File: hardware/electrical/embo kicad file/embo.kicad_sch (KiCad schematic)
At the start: 107 parts, among them J1 24 V PSU input, J10 Conn_01x14, J11 Conn_01x03, J12 Conn_Coaxial, J13 LED Panel, J14 Conn_Coaxial, J2 USB_C_Receptacle_USB2.0_16P, J3 Motor 1 coil A, J4 Motor 1 coil B, J5 Motor 2 coil A, J6 Motor 2 coil B, J7 raspberry pi UART, J8 motor 1, J9 motor 2, Q1 AO3401, U1 TMC2209-LA, U2 ESP32-S3-WROOM-1, U3 AMS1117-3.3, U4 TMC2209-LA, U5 LM2596S-5, U6 OPA2354, U7 OPA2354, U8 AD9833xRM

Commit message: updated
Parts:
- removed Q1: AO3401, symbol Transistor_FET:Q_PMOS_GSD
- added Q2: AO4407A, AO4407A:SOIC127P600X175-8N, symbol AO4407A:AO4407A
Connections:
- net at R5.1: now also Q2.4
- net at J1.1 (Pin_1): now also Q2.5, Q2.6, Q2.7, Q2.8
- net at D1.2 (A), F1.1: now also Q2.1, Q2.2, Q2.3
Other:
- moved on the sheet: R5

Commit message: schematic and pcb docs update
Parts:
- removed J3: Motor 1 coil A, symbol Connector_Generic:Conn_01x02
- removed J4: Motor 1 coil B, symbol Connector_Generic:Conn_01x02
- removed J5: Motor 2 coil A, symbol Connector_Generic:Conn_01x02
- removed J6: Motor 2 coil B, symbol Connector_Generic:Conn_01x02
- added J3, J4: Conn_01x06_Socket, symbol Connector:Conn_01x06_Socket
- Q2: footprint AO4407A:SOIC127P600X175-8N -> Package_SO:SOIC-8_3.9x4.9mm_P1.27mm
- U6, U7: footprint OPA2354AQDGKRQ1:SOP65P490X110-8N -> Package_SO:SOIC-8_3.9x4.9mm_P1.27mm

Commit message: update schematic and PCb docs
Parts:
- removed 10Ω111: R, symbol Device:R
- removed 1nF1: C, symbol Device:C
- removed C1, C2, C3, C6, C8, C9: 100nF, symbol Device:C
- removed C4, C5: 100µF, symbol Device:C
- removed D1: D_Zener, symbol Device:D_Zener
- removed J1: 24 V PSU input, symbol Connector_Generic:Conn_01x02
- removed J11: Conn_01x03, symbol Connector_Generic:Conn_01x03
- removed J7: raspberry pi UART, symbol Connector_Generic:Conn_01x04
- removed R10, R11, R14, R23, R24: 10kΩ, symbol Device:R
- added C36: 100µF, symbol Device:C
- added C37, C40, C41: 100nF, Capacitor_SMD:C_0402_1005Metric, symbol Device:C
- added C38, C39: 100uF, symbol Device:C_Polarized
- added C50: 1nF, Capacitor_SMD:C_0402_1005Metric, symbol Device:C
- added D5: SMBJ28A, Diode_SMD:D_SMA, symbol Device:D_Zener
- added D7: BZX84C15, Package_TO_SOT_SMD:SOT-23, symbol Device:D_Zener
- added J10: BTN UP, Connector_JST:JST_XH_B2B-XH-A_1x02_P2.50mm_Vertical, symbol Connector_Generic:Conn_01x02
- added J11: BTN DOWN, Connector_JST:JST_XH_B2B-XH-A_1x02_P2.50mm_Vertical, symbol Connector_Generic:Conn_01x02
- added J12: BTN SELECT, Connector_JST:JST_XH_B2B-XH-A_1x02_P2.50mm_Vertical, symbol Connector_Generic:Conn_01x02
- added J14: 24 V PSU input, TerminalBlock_Phoenix:TerminalBlock_Phoenix_PT-1,5-2-3.5-H_1x02_P3.50mm_Horizontal, symbol Connector_Generic:Conn_01x02
- added J3: UART to RPi, Connector_JST:JST_XH_B3B-XH-A_1x03_P2.50mm_Vertical, symbol Connector:Conn_01x03_Pin
- added R37: 100Ω, Resistor_SMD:R_0402_1005Metric_Pad0.72x0.64mm_HandSolder, symbol Device:R
- added R38, R39, R40, R41: 10kΩ, Resistor_SMD:R_0402_1005Metric_Pad0.72x0.64mm_HandSolder, symbol Device:R
- added SW1, SW2: SW_Push, Button_Switch_SMD:SW_SPST_EVQP2_MiddlePushTravel_H2.5mm, symbol Switch:SW_Push
- 100nF1: value C -> 100nF; footprint (none) -> Capacitor_SMD:C_0402_1005Metric
- 100nF2: value C2 -> 100nF; footprint (none) -> Capacitor_SMD:C_0402_1005Metric
- C10: value 100nF -> 1uF
- C12, C15, C17, C18, C20, C21, C22, C23, C25, C27, C29, C30, C31, C32, C35: footprint (none) -> Capacitor_SMD:C_0402_1005Metric
- C14: value 100µF -> 100nF; footprint (none) -> Capacitor_SMD:C_0402_1005Metric
- C19: value 100µF -> 220uF
- D2: renamed from D5; value D2 -> BAT54; footprint (none) -> Diode_SMD:D_SOD-123
- D4: value 1N5822 -> SS34A; footprint (none) -> Diode_SMD:D_SMA
- D6: renamed from D3; footprint Diode_THT:D_DO-41_SOD81_P10.16mm_Horizontal -> Diode_SMD:D_SOD-123
- F1: footprint (none) -> Fuse:Fuse_1812_4532Metric_Pad1.30x3.40mm_HandSolder
- J1: renamed from J12; footprint (none) -> Connector_Coaxial:SMA_Molex_73251-1153_EdgeMount_Horizontal
- J13: renamed from J2; footprint (none) -> Connector_USB:USB_C_Receptacle_HRO_TYPE-C-31-M-12
- J2: renamed from J14; footprint (none) -> Connector_Coaxial:SMA_Molex_73251-1153_EdgeMount_Horizontal
- J4: renamed from J3; value Conn_01x06_Socket -> JSTXH 6pin Socket 1; footprint (none) -> Connector_JST:JST_XH_B6B-XH-A_1x06_P2.50mm_Vertical
- J5: renamed from J4; value Conn_01x06_Socket -> JSTXH 6pin Socket 2; footprint (none) -> Connector_JST:JST_XH_B6B-XH-A_1x06_P2.50mm_Vertical
- J6: renamed from J8; footprint (none) -> Connector_JST:JST_XH_B2B-XH-A_1x02_P2.50mm_Vertical
- J7: renamed from J9; footprint (none) -> Connector_JST:JST_XH_B2B-XH-A_1x02_P2.50mm_Vertical
- J8: renamed from J13; footprint (none) -> Connector_JST:JST_XH_B2B-XH-A_1x02_P2.50mm_Vertical
- J9: renamed from J10; footprint (none) -> Connector_PinSocket_2.54mm:PinSocket_1x14_P2.54mm_Vertical
- LED_stat1: renamed from D2; footprint (none) -> LED_SMD:LED_0805_2012Metric
- R1, R12, R13, R17, R18, R19, R2, R21, R22, R25, R26, R27, R28, R29, R3, R30, R31, R32, R33, R34, R35, R36, R4, R5, R6, R9: footprint (none) -> Resistor_SMD:R_0402_1005Metric_Pad0.72x0.64mm_HandSolder
- R15, R16, R7, R8: footprint (none) -> Resistor_SMD:R_2512_6332Metric
- R20: value 100Ω -> 10kΩ; footprint (none) -> Resistor_SMD:R_0402_1005Metric_Pad0.72x0.64mm_HandSolder
- renumbered D7 to D1, D6 to D3, U6 to IC1, U7 to IC2, Q2 to Q1, U2 to U1, U5 to U2, U8 to U4, U1 to U5, U4 to U6
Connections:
- net +24V: now also C16.1, C36.1, C38.1, C39.1, D5.1 (K); no longer C14.1
- net +3V3: now also R2.1, R21.1, R25.2, R4.1, R38.1, R40.2, R41.2; no longer C32.1, R21.2, R25.1
- net +5V: now also L1.1; no longer L1.2
- net BTN_DOWN: now also C40.1, J11.2 (Pin_2); no longer C10.2
- net BTN_SELECT: now also C41.1, J12.2 (Pin_2)
- net BTN_UP: now also C32.1, J10.2 (Pin_2)
- net GND: now also 100nF1.2, C10.2, C34.1, D4.2 (A), R29.2, C36.2, C37.2, C38.2, C39.2, C40.2, C41.2, C50.2, D5.2 (A), J10.1 (Pin_1), J11.1 (Pin_1), J12.1 (Pin_1), J14.2 (Pin_2), J3.1 (Pin_1), R37.1, R39.2, SW1.2, SW2.2; no longer C10.1, C34.2, D4.1 (K), R2.2, R20.1, R29.1, R4.2
- net M1_A1: now also J4.1 (Pin_1)
- net M1_A2: now also J4.3 (Pin_3)
- net M1_B1: now also J4.4 (Pin_4)
- net M1_B2: now also J4.6 (Pin_6)
- net M2_A1: now also J5.1 (Pin_1)
- net M2_A2: now also J5.3 (Pin_3)
- net M2_B1: now also J5.4 (Pin_4)
- net M2_B2: now also J5.6 (Pin_6)
- net STAGE1_OUT: now also C21.1, R35.2; no longer C21.2, R35.1
- net TFT_RST: now also R25.1; no longer R25.2
- net TX_AMP_IN: now also C35.1, U4.10 (VOUT); no longer C35.2, IC1.3 (+INA), IC1.5 (+INB)
- net UART_RX: now also J3.2 (Pin_2)
- net UART_TX: now also J3.3 (Pin_3)
- net USB_D+: now also J13.B6 (D+)
- net USB_D-: now also J13.B7 (D-)
- net at IC2.5 (+INB), R22.1: now also C21.2, R21.2; no longer C21.1, R21.1
- net at U6.20 (STDBY): now also R4.2
- net at IC2.2 (-INA), R26.2: no longer names the net of IC2.2 (-INA), R26.2
- net at IC2.2 (-INA), R26.2: now also R35.1; no longer R35.2
- net at U1.27 (IO0): now also C14.1, R41.1, SW2.1
- net at U1.3 (EN): now also C10.1, R40.1, SW1.1
- net at Q1.1, Q1.2, Q1.3: now also D7.1 (K), J14.1 (Pin_1); no longer F1.1
- net at Q1.4, R5.1: now also D7.2 (A)
- net at Q1.5, Q1.6, Q1.7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: now also F1.1
- net at U4.1 (COMP): now also C34.2; no longer C34.1
- net at C20.2, IC2.3 (+INA), R28.2: now also R29.1; no longer R29.2
- net at U5.11 (DIAG): no longer R2.1
- net at U5.12 (INDEX): no longer R4.1
- net at U5.20 (STDBY): now also R2.2
- net at U5.6 (VCP): now also C37.1
- net at IC1.2 (-INA), R33.2: now also R37.2; no longer R20.2
- net MCLK: no longer names the net of U4.5 (MCLK)
- new net: D4.1 (K), L1.2, R20.1, U2.2 (OUT)
- new net: C50.1, R20.2
- new net: C35.2, IC1.3 (+INA), IC1.5 (+INB), R38.2, R39.1
- no-connect marks 30 -> 31
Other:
- note added: "1"
- note added: "1.65V bias"
- note added: "24V to 5V Buck Converter"
- note added: "29/06/2026"
- note added: "AC coupling (blocks DC)"
- note added: "AD9833 Signal Gen"
- note added: "Boot Circuit"
- note added: "EMBO MCU Board v1.0"
- note added: "EN reset circuit"
- note added: "HF/LF power decoupling"
- note added: "LED"
- note added: "MOSFET for reverse current switch"
- note added: "Micro-controller"
- note added: "Motor Drivers"
- note added: "RC filter"
- note added: "RX Chain"
- note added: "Screen Buttons"
- note added: "Screen Connector"
- note added: "TL matching (reflected wave dampener)"
- note added: "TX Chain"
- note added: "UART address: 0"
- note added: "UART address: 1"
- note added: "UI"
- note added: "Ultrasonic Attenuation Spectroscopy Analog Signal Generation & Processing"
- note added: "VCP cap to be within 2mm of IC"
- note added: "bleed resistor"
- note added: "catch diode"
- note added: "charge detection"
- note added: "clamps Vgs to safe level"
- note added: "clamps voltage transients above 28V"
- note added: "current sense resistors"
- note added: "debounce capacitors"
- note added: "diode clamp protection"
- note added: "envelope rectifier diode"
- note added: "internal voltage reference (data sheet requirement)"
- note added: "note: only channel 1 is used channel 2 is kept stable by setting it as a unity gain follower"
- note added: "power decoupling"
- note added: "pre ADC filter (rec by espressif)"
- note added: "pre ADC processing"
- note added: "snubber (damp HF)"
- note added: "stage 1 set gain to 3.9"
- note added: "stage 1 set gain to 9.1"
- note added: "stage 2 set gain to 9.1"
- note added: "switching inductor"
- note added: "to motor coils"
- note added: "unity gain follower (tie off the unused channel)"
- note added: "v2.2"
- note removed: "5V Buck converter part"
- note removed: "AD9833"
- note removed: "Screen connector"
- note removed: "Ultrasonic Attenuation Spectroscopy"
- note removed: "screen button"
- moved on the sheet: 100nF2, C7, D1, D3, D4, IC1, IC2, J1, J2, J4, J5, J8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

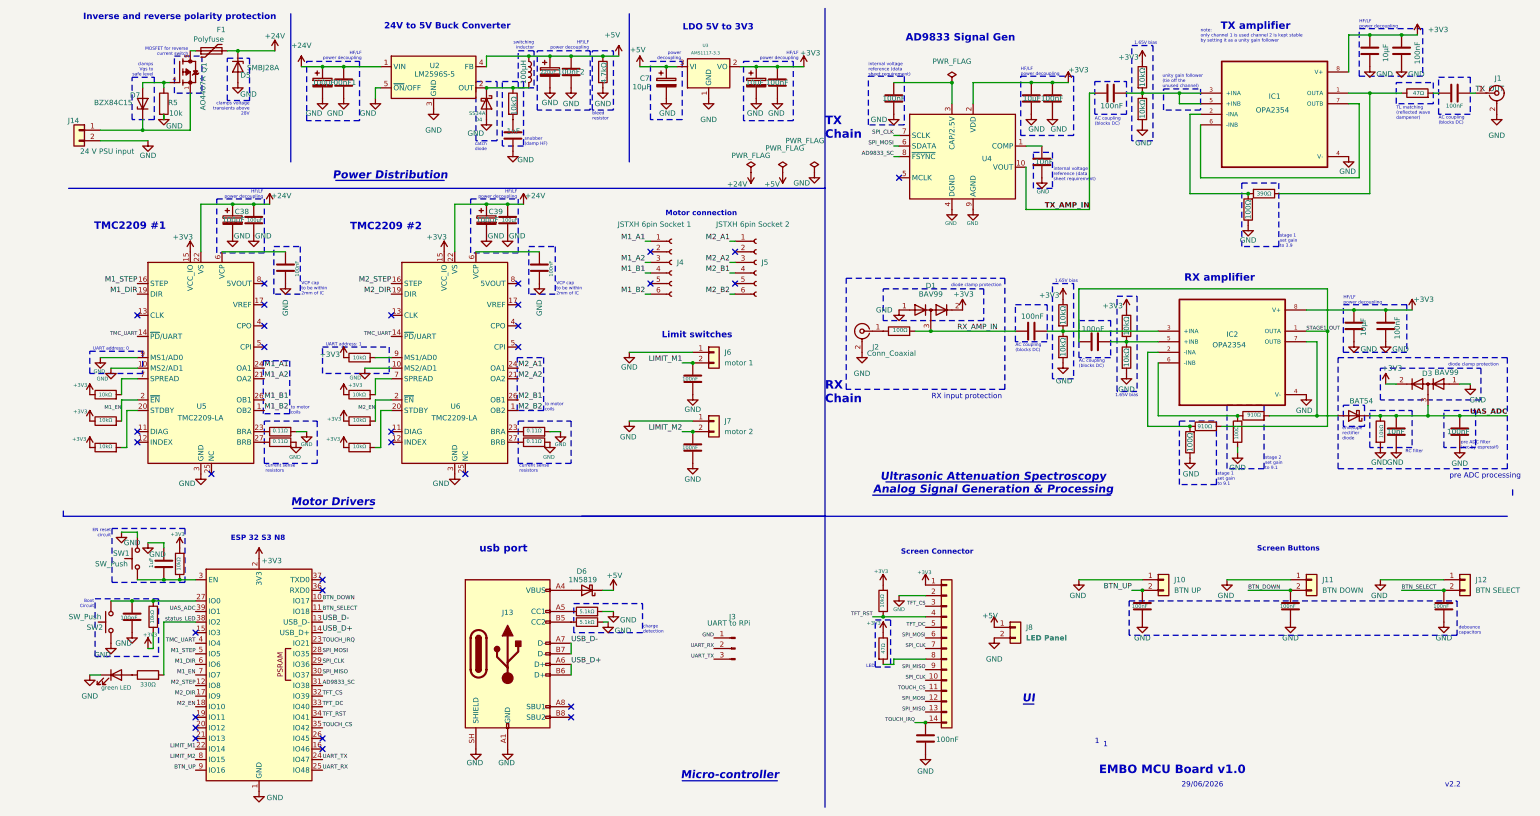
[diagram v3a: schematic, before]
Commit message: PCB Placement Update
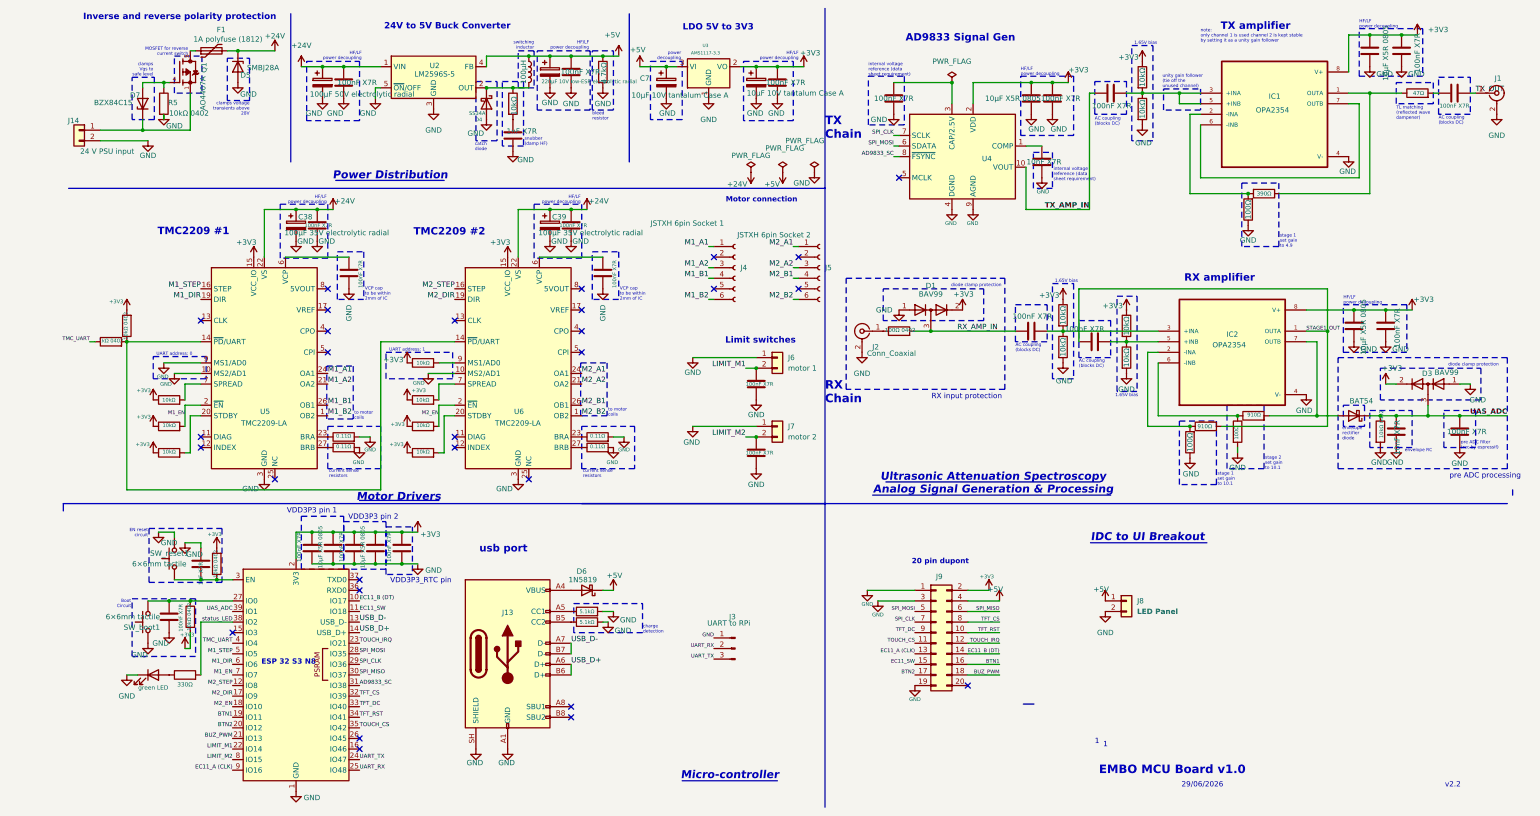
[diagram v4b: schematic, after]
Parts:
- removed C14: 100nF, Capacitor_SMD:C_0402_1005Metric, symbol Device:C
- removed J10: BTN UP, Connector_JST:JST_XH_B2B-XH-A_1x02_P2.50mm_Vertical, symbol Connector_Generic:Conn_01x02
- removed J11: BTN DOWN, Connector_JST:JST_XH_B2B-XH-A_1x02_P2.50mm_Vertical, symbol Connector_Generic:Conn_01x02
- removed J12: BTN SELECT, Connector_JST:JST_XH_B2B-XH-A_1x02_P2.50mm_Vertical, symbol Connector_Generic:Conn_01x02
- removed J9: Conn_01x14, Connector_PinSocket_2.54mm:PinSocket_1x14_P2.54mm_Vertical, symbol Connector_Generic:Conn_01x14
- removed R25: 10kΩ, Resistor_SMD:R_0402_1005Metric_Pad0.72x0.64mm_HandSolder, symbol Device:R
- removed R30: 47Ω, Resistor_SMD:R_0402_1005Metric_Pad0.72x0.64mm_HandSolder, symbol Device:R
- added C28: 10µF X5R 0805, Capacitor_SMD:C_0805_2012Metric, symbol Device:C
- added C29: 100nF X7R, Capacitor_SMD:C_0402_1005Metric_Pad0.74x0.62mm_HandSolder, symbol Device:C
- added J9: Conn_02x10_Odd_Even, Connector_IDC:IDC-Header_2x10_P2.54mm_Vertical, symbol Connector_Generic:Conn_02x10_Odd_Even
- added R_PDN_UP1: 10kΩ 0402, Resistor_SMD:R_0402_1005Metric_Pad0.72x0.64mm_HandSolder, symbol Device:R
- added R_UART1: 1kΩ 0402, Resistor_SMD:R_0402_1005Metric_Pad0.72x0.64mm_HandSolder, symbol Device:R
- C10: value 1uF -> 1µF X7R; footprint (none) -> Capacitor_SMD:C_0402_1005Metric_Pad0.74x0.62mm_HandSolder
- C11, C7: value 10µF -> 10µF 10V tantalum Case A; footprint (none) -> Capacitor_Tantalum_SMD:CP_EIA-3216-18_Kemet-A_HandSolder
- C12, C15, C17, C18, C20, C21, C22, C23, C25, C27, C30, C31, C35, C37, C40, C41: value 100nF -> 100nF X7R; footprint Capacitor_SMD:C_0402_1005Metric -> Capacitor_SMD:C_0402_1005Metric_Pad0.74x0.62mm_HandSolder
- C13, C36: value 100µF -> 100nF X7R; footprint (none) -> Capacitor_SMD:C_0402_1005Metric_Pad0.74x0.62mm_HandSolder
- C16: value 100µF -> 100µF 50V electrolytic radial; footprint (none) -> Capacitor_THT:C_Radial_D8.0mm_H11.5mm_P3.50mm
- C19: value 220uF -> 220µF 10V low-ESR electrolytic radial; footprint (none) -> Capacitor_THT:C_Radial_D8.0mm_H11.5mm_P3.50mm
- C24, C26, C33: value 10µF -> 10µF X5R 0805; footprint (none) -> Capacitor_SMD:C_0805_2012Metric
- C32: value 100nF -> 10µF X5R 0805; footprint Capacitor_SMD:C_0402_1005Metric -> Capacitor_SMD:C_0805_2012Metric
- C34: value 10nF -> 10nF X7R; footprint (none) -> Capacitor_SMD:C_0402_1005Metric
- C38, C39: value 100uF -> 100µF 35V electrolytic radial; footprint (none) -> Capacitor_THT:C_Radial_D6.3mm_H11.0mm_P2.50mm
- C50: value 1nF -> 1nF X7R; footprint Capacitor_SMD:C_0402_1005Metric -> Capacitor_SMD:C_0402_1005Metric_Pad0.74x0.62mm_HandSolder
- C_adc1: renamed from C29; value 100nF -> 100nF X7R; footprint Capacitor_SMD:C_0402_1005Metric -> Capacitor_SMD:C_0402_1005Metric_Pad0.74x0.62mm_HandSolder
- C_env1: renamed from C28; value 10nF -> 10nF X7R; footprint (none) -> Capacitor_SMD:C_0402_1005Metric
- Cbuck1: renamed from 100nF1; value 100nF -> 100nF X7R; footprint Capacitor_SMD:C_0402_1005Metric -> Capacitor_SMD:C_0402_1005Metric_Pad0.74x0.62mm_HandSolder
- Cbuckout1: renamed from 100nF2; value 100nF -> 100nF X7R; footprint Capacitor_SMD:C_0402_1005Metric -> Capacitor_SMD:C_0402_1005Metric_Pad0.74x0.62mm_HandSolder
- F1: value Polyfuse -> 1A polyfuse (1812)
- R40, R41: value 10kΩ -> 10kΩ 0402
- R5: value 10k -> 10kΩ 0402
- R_env1: renamed from R34; value 10kΩ -> 10kΩ 0402
- R_in1: renamed from R36; value 100Ω -> 100Ω 0402
- SW_boot1: renamed from SW2; value SW_Push -> 6×6mm tactile
- SW_reset1: renamed from SW1; value SW_Push -> 6×6mm tactile
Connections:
- net +3V3: now also C22.2, C32.2, C40.2, C28.2, C29.2, J9.2 (Pin_2), R_PDN_UP1.2
- net +5V: now also J9.4 (Pin_4)
- net GND: now also C22.1, C32.1, C40.1, C28.1, C29.1, J9.1 (Pin_1), J9.19 (Pin_19), J9.3 (Pin_3); no longer C22.2, C32.2, C40.2
- net SPI_CLK: now also J9.7 (Pin_7)
- net SPI_MISO: now also J9.6 (Pin_6)
- net SPI_MOSI: now also J9.5 (Pin_5)
- net TFT_CS: now also J9.8 (Pin_8)
- net TFT_DC: now also J9.9 (Pin_9)
- net TFT_RST: now also J9.10 (Pin_10)
- net TMC_UART: now also R_UART1.1; no longer U5.14 (~{PD}/UART), U6.14 (~{PD}/UART)
- net TOUCH_CS: now also J9.11 (Pin_11)
- net TOUCH_IRQ: now also J9.12 (Pin_12); no longer C22.1
- net at R41.1, SW_boot1.1, U1.27 (IO0): now also C41.1
- net BTN1: now reaches U1.19 (IO11)
- net BTN1: now also J9.16 (Pin_16)
- net BTN2: now reaches U1.20 (IO12)
- net BTN2: now also J9.17 (Pin_17)
- net BUZ_PWM: now reaches U1.21 (IO13)
- net BUZ_PWM: now also J9.18 (Pin_18)
- net BTN_DOWN renamed EC11_B (DT)
- net EC11_B (DT): now also J9.14 (Pin_14); no longer C40.1
- net BTN_SELECT renamed EC11_SW
- net EC11_SW: now also J9.15 (Pin_15); no longer C41.1
- net BTN_UP renamed EC11_A (CLK)
- net EC11_A (CLK): now also J9.13 (Pin_13); no longer C32.1
- new net: R_PDN_UP1.1, R_UART1.2, U5.14 (~{PD}/UART), U6.14 (~{PD}/UART)
- no-connect marks 31 -> 29
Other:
- note added: "20 pin dupont"
- note added: "IDC to UI Breakout"
- note added: "VDD3P3 pin 1"
- note added: "VDD3P3 pin 2"
- note added: "VDD3P3_RTC pin"
- note added: "envelope RC"
- note added: "stage 1 set gain to 10.1"
- note added: "stage 1 set gain to 4.9"
- note added: "stage 2 set gain to 10.1"
- note removed: "LED"
- note removed: "RC filter"
- note removed: "Screen Buttons"
- note removed: "Screen Connector"
- note removed: "UI"
- note removed: "debounce capacitors"
- note removed: "stage 1 set gain to 3.9"
- note removed: "stage 1 set gain to 9.1"
- note removed: "stage 2 set gain to 9.1"
- moved on the sheet: C38, C39, J4, J5, J6, J7, J8, SW_boot1, SW_reset1, U5, U6

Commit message: PCB layout update
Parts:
- L1: footprint (none) -> Inductor_SMD:L_Bourns_SRR1260
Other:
- note added: "20 pin IDC Socket"
- note removed: "20 pin dupont"
- moved on the sheet: J8
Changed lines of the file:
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@@
 	(text "ESP 32 S3 N8\n"
 		(exclude_from_sim no)
-		(at 65.532 169.672 0)
+		(at 67.056 177.546 0)
 		(effects
 			(font
@@
 	(text "Micro-controller"
 		(exclude_from_sim no)
-		(at 171.45 196.85 0)
+		(at 97.79 200.66 0)
 		(effects
 			(font
@@
 		)
 	)
-	(text "20 pin dupont"
+	(text "20 pin IDC Socket"
 		(exclude_from_sim no)
 		(at 221.996 145.542 0)
@@
 	(polyline
 		(pts
-			(xy 182.88 198.12) (xy 160.02 198.12)
+			(xy 109.22 201.93) (xy 86.36 201.93)
 		)
 		(stroke
@@
 	(symbol
 		(lib_id "power:GND")
-		(at 261.62 157.48 0)
+		(at 166.37 179.07 0)
 		(unit 1)
 		(body_style 1)
@@
 		(fields_autoplaced yes)
 		(property "Reference" "#PWR0103"
-			(at 261.62 163.83 0)
+			(at 166.37 185.42 0)
 			(hide yes)
 			(show_name no)
@@
 		)
 		(property "Value" "GND"
-			(at 261.62 162.56 0)
+			(at 166.37 184.15 0)
 			(show_name no)
 			(do_not_autoplace no)
@@
 		)
 		(property "Footprint" ""
-			(at 261.62 157.48 0)
+			(at 166.37 179.07 0)
 			(hide yes)
 			(show_name no)
@@
 		)
 		(property "Datasheet" ""
-			(at 261.62 157.48 0)
+			(at 166.37 179.07 0)
 			(hide yes)
 			(show_name no)
@@
 		)
 		(property "Description" "Power symbol creates a global label with name \"GND\" , ground"
-			(at 261.62 157.48 0)
+			(at 166.37 179.07 0)
 			(hide yes)
 			(show_name no)
@@
 	(symbol
 		(lib_id "Connector_Generic:Conn_01x02")
-		(at 266.7 154.94 0)
+		(at 171.45 176.53 0)
 		(unit 1)
 		(body_style 1)
@@
 		(fields_autoplaced yes)
 		(property "Reference" "J8"
-			(at 269.24 154.9399 0)
+			(at 173.99 176.5299 0)
 			(show_name no)
 			(do_not_autoplace no)
@@
 		)
 		(property "Value" "LED Panel"
-			(at 269.24 157.48 0)
+			(at 173.99 179.07 0)
 			(show_name no)
 			(do_not_autoplace no)
@@
 		)
 		(property "Footprint" "Connector_JST:JST_XH_B2B-XH-A_1x02_P2.50mm_Vertical"
-			(at 266.7 154.94 0)
+			(at 171.45 176.53 0)
 			(hide yes)
 			(show_name no)
@@
 		)
 		(property "Datasheet" ""
-			(at 266.7 154.94 0)
+			(at 171.45 176.53 0)
 			(hide yes)
 			(show_name no)
@@
 		)
 		(property "Description" "Generic connector, single row, 01x02, script generated (kicad-library-utils/schlib/autogen/connector/)"
-			(at 266.7 154.94 0)
+			(at 171.45 176.53 0)
 			(hide yes)
 			(show_name no)
@@
 			)
 		)
-		(property "Footprint" ""
+		(property "Footprint" "Inductor_SMD:L_Bourns_SRR1260"
 			(at 123.19 27.94 0)
 			(hide yes)
@@
 	(symbol
 		(lib_id "power:+5V")
-		(at 261.62 154.94 0)
+		(at 166.37 176.53 0)
 		(unit 1)
 		(body_style 1)
@@
 		(dnp no)
 		(property "Reference" "#PWR0102"
-			(at 261.62 158.75 0)
+			(at 166.37 180.34 0)
 			(hide yes)
 			(show_name no)
@@
 		)
 		(property "Value" "+5V"
-			(at 260.604 152.146 0)
+			(at 165.354 173.736 0)
 			(show_name no)
 			(do_not_autoplace no)
@@
 		)
 		(property "Footprint" ""
-			(at 261.62 154.94 0)
+			(at 166.37 176.53 0)
 			(hide yes)
 			(show_name no)
@@
 		)
 		(property "Datasheet" ""
-			(at 261.62 154.94 0)
+			(at 166.37 176.53 0)
 			(hide yes)
 			(show_name no)
@@
 		)
 		(property "Description" "Power symbol creates a global label with name \"+5V\""
-			(at 261.62 154.94 0)
+			(at 166.37 176.53 0)
 			(hide yes)
 			(show_name no)
